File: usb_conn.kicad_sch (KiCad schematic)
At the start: 0 parts

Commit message: lots
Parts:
- added FB4: FerriteBead, Resistor_SMD:R_0402_1005Metric, symbol Device:FerriteBead
- added U6: TPUSBLC6-4SC6, Package_TO_SOT_SMD:SOT-23-6_Handsoldering, symbol Library:TPUSBLC6-4SC6
- added USB1: HYCW498-USBC16-735B, C42400252:USB-C-SMD_HYCW498-USBC16-735B, symbol C42400252:HYCW498-USBC16-735B
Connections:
- net USB.D+: now also U6.1
- net USB.D-: now also U6.6
- new net EXT_VBUS: FB4.2, U6.5
- new net GND: U6.2 (VSS)
- new net VBUS: FB4.1
- no-connect marks 0 -> 2
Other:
- note added: "TODO: source USB-C conn"

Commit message: almost finished usb
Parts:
- added C127: 100n 10V, Capacitor_SMD:C_0402_1005Metric, symbol Device:C
- added C128: 10u 10V, Capacitor_SMD:C_0805_2012Metric, symbol Device:C
- added R92, R93: 5.1k, Resistor_SMD:R_0402_1005Metric, symbol Device:R
- added TP172, TP173, TP174, TP175, TP176, TP178, TP179: TestPoint, TestPoint:TestPoint_THTPad_D1.0mm_Drill0.5mm, symbol Connector:TestPoint
- added TP177: TestPoint_Alt, TestPoint:TestPoint_THTPad_1.0x1.0mm_Drill0.5mm, symbol Connector:TestPoint_Alt
- added U13: DLM0NSN500HY2D, C913480:FILTER-SMD_4P-L0.8-W0.6-TL_DLP0NSC280HL2L, symbol C913480:DLM0NSN500HY2D
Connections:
- net EXT_VBUS: now also USB1.A4B9 (VBUS), USB1.B4A9 (VBUS), TP172.1
- net GND: now also USB1.1 (SHELL), USB1.2 (SHELL), USB1.3 (SHELL), USB1.4 (SHELL), USB1.A1B12 (GND), USB1.B1A12 (GND), C127.2, C128.2, R92.1, R93.1, TP177.1
- net USB.D+: now also U13.4; no longer U6.1
- net USB.D-: now also U13.1; no longer U6.6
- net EXT_USB_CC1: now reaches U6.3
- net EXT_USB_CC1: now also USB1.A5 (CC1), R92.2, TP173.1
- net EXT_USB_CC2: now reaches U6.4
- net EXT_USB_CC2: now also USB1.B5 (CC2), R93.2, TP174.1
- net EXT_USB_D+: now reaches USB1.A6 (DP1)
- net EXT_USB_D+: now also U6.1, USB1.B6 (DP2), TP175.1, U13.3
- net EXT_USB_D-: now reaches USB1.A7 (DN1)
- net EXT_USB_D-: now also U6.6, USB1.B7 (DN2), TP176.1, U13.2
- net NC_USB_SBU1: now reaches USB1.A8 (SBU1)
- net NC_USB_SBU1: now also TP178.1
- net NC_USB_SBU2: now reaches USB1.B8 (SBU2)
- net NC_USB_SBU2: now also TP179.1
- net VBUS renamed +5V_USB
- net +5V_USB: now also C127.1, C128.1
- no-connect marks 2 -> 0
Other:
- note added: "USB-C Connector"
- note removed: "TODO: source USB-C conn"
- moved on the sheet: FB4, U6

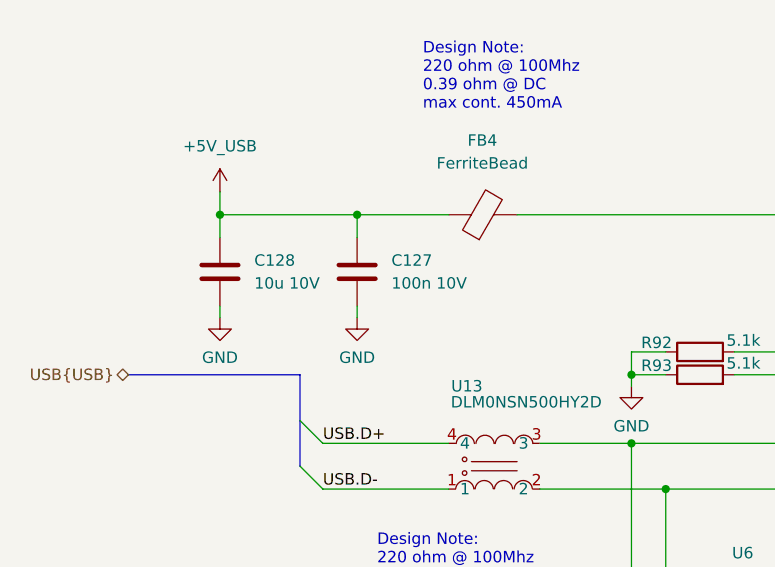
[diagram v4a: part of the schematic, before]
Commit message: did a bunch of bom matching to lcsc
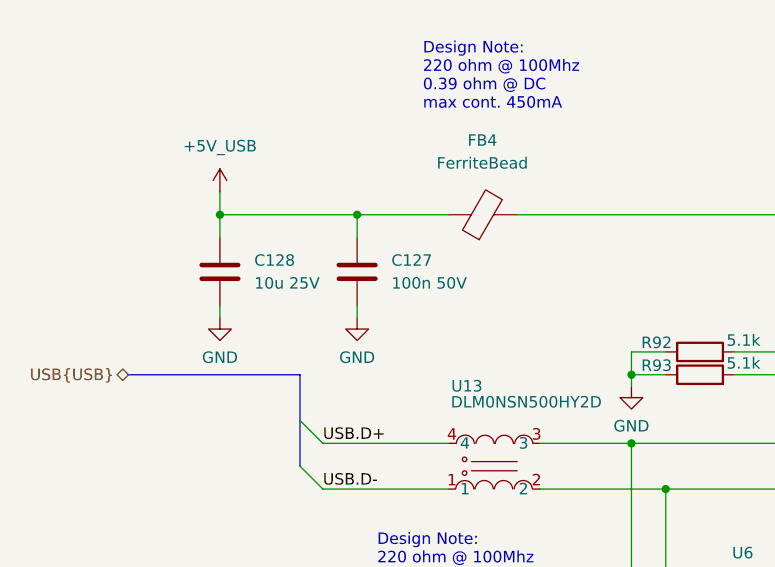
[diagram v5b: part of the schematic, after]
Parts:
- C127: value 100n 10V -> 100n 50V; LCSC (none) -> C307331; LCSC Basic/Pref (none) -> x; LCSC Part (none) -> C307331
- C128: value 10u 10V -> 10u 25V; LCSC (none) -> C15850; LCSC Basic/Pref (none) -> x; LCSC Part (none) -> C15850
- R92, R93: LCSC (none) -> C25905; LCSC Basic/Pref (none) -> x; LCSC Part (none) -> C25905
- TP172, TP173, TP174, TP175, TP176, TP177, TP178, TP179: now left out of the parts list
- U6: LCSC Part (none) -> C558419
